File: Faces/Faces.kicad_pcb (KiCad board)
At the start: 6 copper layers, 120.8 x 142.1 mm, 92 parts

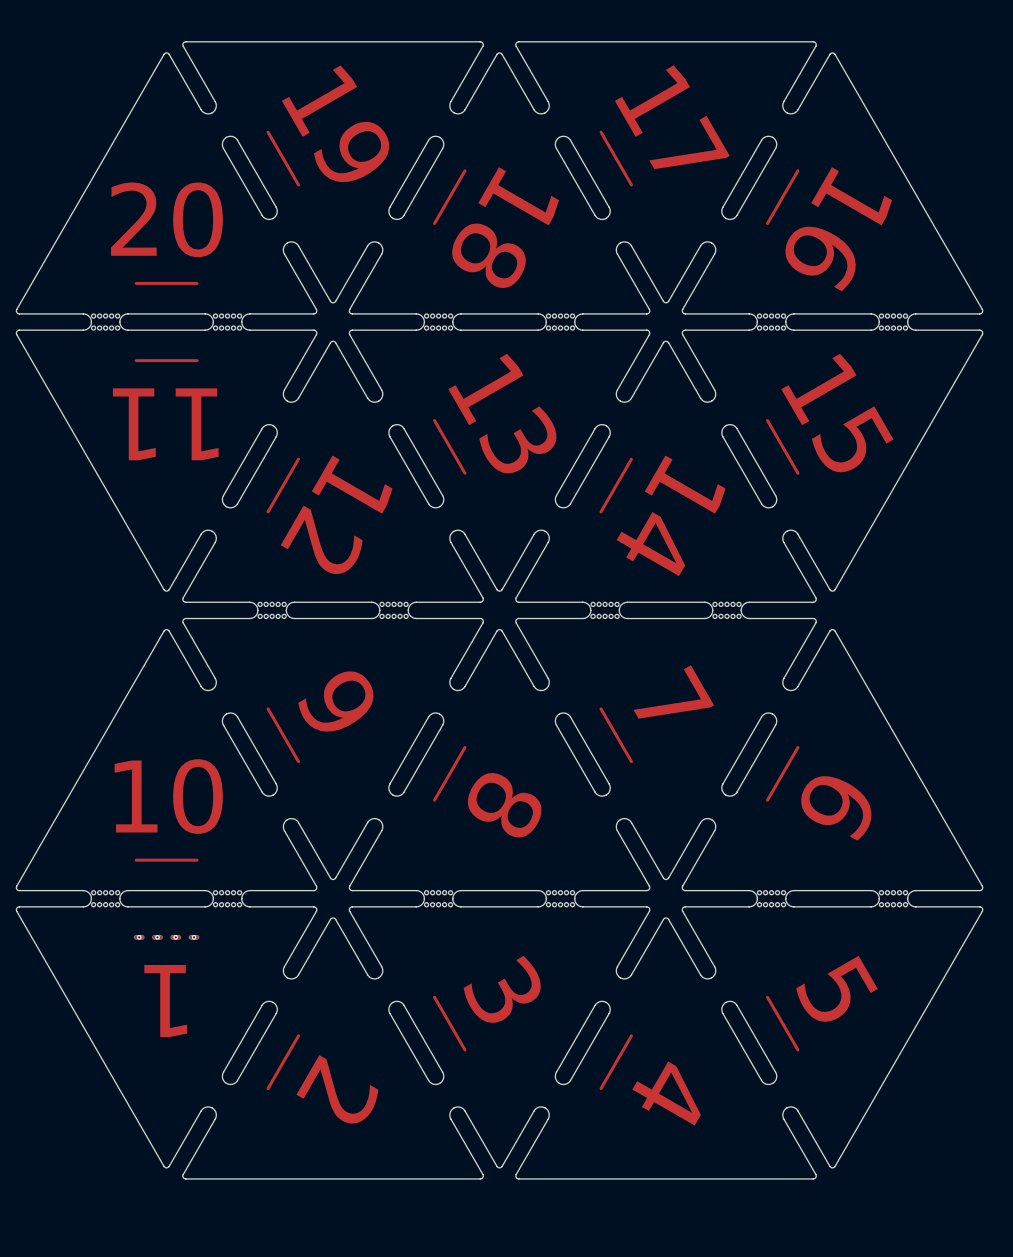
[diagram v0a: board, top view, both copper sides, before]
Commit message: Re-tool faces. It costs nothing to add the extra panelization holes. They bill this as 20 designs regardless.
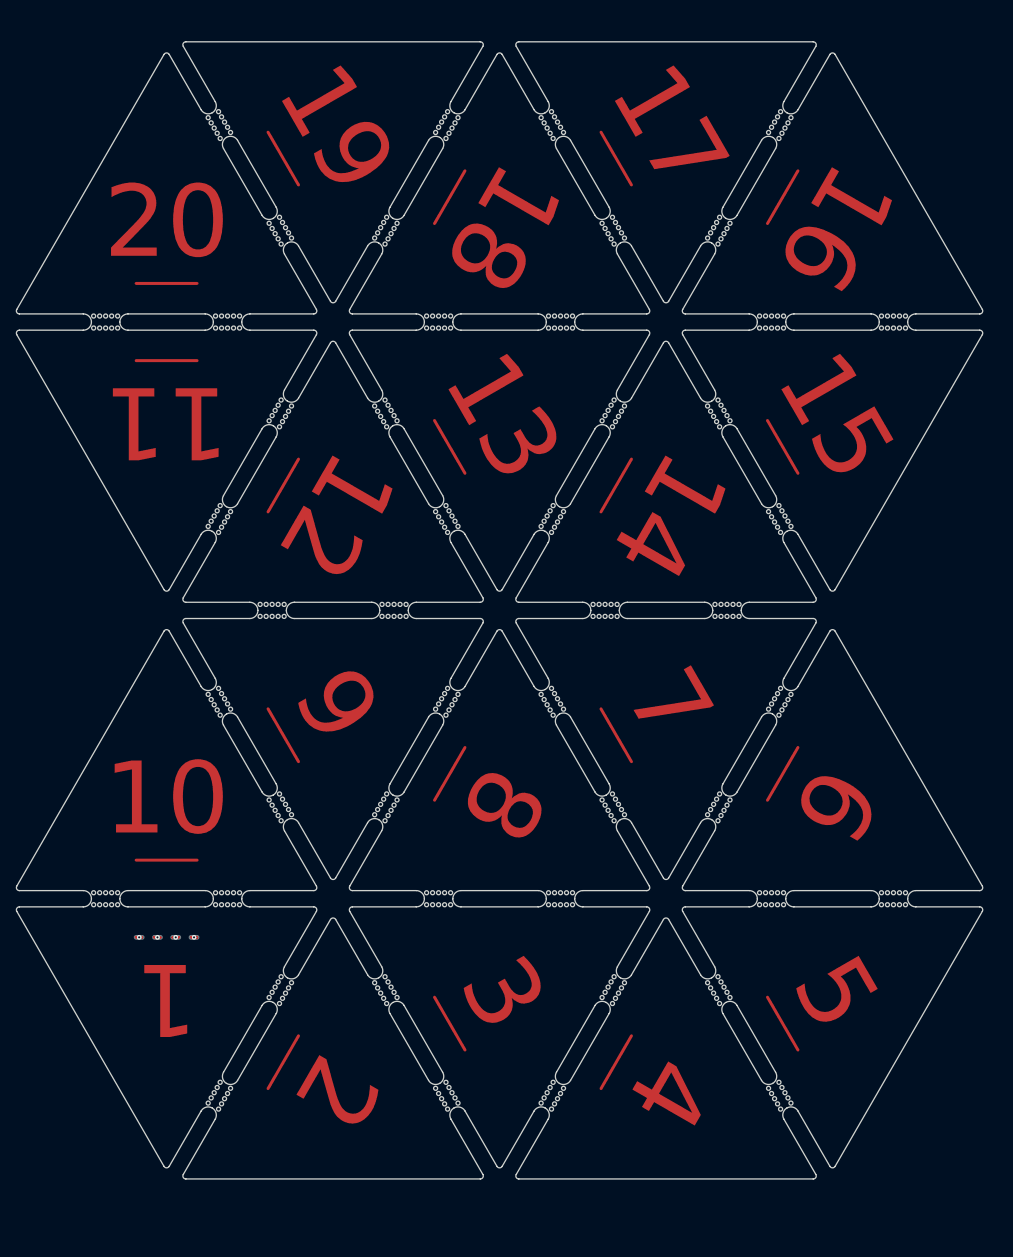
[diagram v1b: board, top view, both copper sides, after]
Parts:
- added mouse-bite-2mm-slot (x2): VAL**, Panelization:mouse-bite-2mm-slot, F.Cu at (78.2, 63.2)
- added mouse-bite-2mm-slot (x2): VAL**, Panelization:mouse-bite-2mm-slot, F.Cu at (127.4, 148.5)
- added mouse-bite-2mm-slot (x2): VAL**, Panelization:mouse-bite-2mm-slot, F.Cu at (65.0, 135.3)
- added mouse-bite-2mm-slot (x2): VAL**, Panelization:mouse-bite-2mm-slot, F.Cu at (85.8, 99.3)
- added mouse-bite-2mm-slot (x2): VAL**, Panelization:mouse-bite-2mm-slot, F.Cu at (65.0, 40.4)
- added mouse-bite-2mm-slot (x2): VAL**, Panelization:mouse-bite-2mm-slot, F.Cu at (65.0, 63.2)
- added mouse-bite-2mm-slot (x2): VAL**, Panelization:mouse-bite-2mm-slot, F.Cu at (127.4, 99.3)
- added mouse-bite-2mm-slot (x2): VAL**, Panelization:mouse-bite-2mm-slot, F.Cu at (106.6, 63.2)
- added mouse-bite-2mm-slot (x2): VAL**, Panelization:mouse-bite-2mm-slot, F.Cu at (57.4, 99.3)
- added mouse-bite-2mm-slot (x2): VAL**, Panelization:mouse-bite-2mm-slot, F.Cu at (57.4, 76.4)
- added mouse-bite-2mm-slot (x2): VAL**, Panelization:mouse-bite-2mm-slot, F.Cu at (106.6, 112.5)
- added mouse-bite-2mm-slot (x2): VAL**, Panelization:mouse-bite-2mm-slot, F.Cu at (99.0, 148.5)
- added mouse-bite-2mm-slot (x2): VAL**, Panelization:mouse-bite-2mm-slot, F.Cu at (85.8, 148.5)
- added mouse-bite-2mm-slot (x2): VAL**, Panelization:mouse-bite-2mm-slot, F.Cu at (57.4, 148.5)
- added mouse-bite-2mm-slot (x2): VAL**, Panelization:mouse-bite-2mm-slot, F.Cu at (85.8, 76.4)
- added mouse-bite-2mm-slot (x2): VAL**, Panelization:mouse-bite-2mm-slot, F.Cu at (119.8, 112.5)
- added mouse-bite-2mm-slot (x2): VAL**, Panelization:mouse-bite-2mm-slot, F.Cu at (119.8, 63.2)
- added mouse-bite-2mm-slot (x2): VAL**, Panelization:mouse-bite-2mm-slot, F.Cu at (106.6, 40.4)
- added mouse-bite-2mm-slot (x2): VAL**, Panelization:mouse-bite-2mm-slot, F.Cu at (78.2, 135.3)
- added mouse-bite-2mm-slot (x2): VAL**, Panelization:mouse-bite-2mm-slot, F.Cu at (127.4, 27.2)
- added mouse-bite-2mm-slot (x2): VAL**, Panelization:mouse-bite-2mm-slot, F.Cu at (119.8, 40.4)
- added mouse-bite-2mm-slot (x2): VAL**, Panelization:mouse-bite-2mm-slot, F.Cu at (65.0, 112.5)
- added mouse-bite-2mm-slot (x2): VAL**, Panelization:mouse-bite-2mm-slot, F.Cu at (85.8, 27.2)
- added mouse-bite-2mm-slot (x2): VAL**, Panelization:mouse-bite-2mm-slot, F.Cu at (127.4, 76.4)
- added mouse-bite-2mm-slot (x2): VAL**, Panelization:mouse-bite-2mm-slot, F.Cu at (119.8, 135.3)
- added mouse-bite-2mm-slot (x2): VAL**, Panelization:mouse-bite-2mm-slot, F.Cu at (57.4, 27.2)
- added mouse-bite-2mm-slot (x2): VAL**, Panelization:mouse-bite-2mm-slot, F.Cu at (99.0, 76.4)
- added mouse-bite-2mm-slot (x2): VAL**, Panelization:mouse-bite-2mm-slot, F.Cu at (99.0, 99.3)
- added mouse-bite-2mm-slot (x2): VAL**, Panelization:mouse-bite-2mm-slot, F.Cu at (106.6, 135.3)
- added mouse-bite-2mm-slot (x2): VAL**, Panelization:mouse-bite-2mm-slot, F.Cu at (99.0, 27.2)
- added mouse-bite-2mm-slot (x2): VAL**, Panelization:mouse-bite-2mm-slot, F.Cu at (78.2, 40.4)
- added mouse-bite-2mm-slot (x2): VAL**, Panelization:mouse-bite-2mm-slot, F.Cu at (78.2, 112.5)
- moved G*** 3.59 mm to (109.5, 93.1), turned to -55 degrees
- moved G*** 3.10 mm to (68.2, 91.4), turned to -65 degrees
- moved G*** 2.73 mm to (60.4, 137.8)
- moved G*** 2.61 mm to (138.9, 103.7), turned to -125 degrees
- moved G*** 2.10 mm to (139.5, 31.4), turned to -125 degrees
- moved G*** 2.07 mm to (108.8, 18.8), turned to -65 degrees
- moved G*** 1.97 mm to (40.6, 111.9), turned to -5 degrees
- moved G*** 1.91 mm to (97.9, 31.2), turned to -125 degrees
- moved G*** 1.84 mm to (67.4, 18.3), turned to -65 degrees
- moved G*** 1.67 mm to (98.0, 103.0), turned to -125 degrees
- moved G*** 1.55 mm to (41.0, 137.4)
- moved G*** 1.03 mm to (77.5, 66.4)
- moved G*** 0.70 mm to (62.2, 64.3)
- moved G*** 0.51 mm to (39.0, 39.5)

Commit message: Somewhere around the first complete prototype. time to change BMS
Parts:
- moved G*** 152.7 mm to (119.2, 161.9), turned to 115 degrees
- moved G*** 149.4 mm to (47.1, 148.8), turned to 55 degrees
- moved G*** 148.4 mm to (147.6, 140.7), turned to 170 degrees
- moved G*** 146.0 mm to (77.8, 161.5), turned to 115 degrees
- moved mouse-bite-2mm-slot 144.9 mm to (129.2, 153.1), turned to 120 degrees
- moved mouse-bite-2mm-slot 144.9 mm to (129.2, 153.1), turned to -60 degrees
- moved mouse-bite-2mm-slot 143.2 mm to (59.1, 153.1), turned to 60 degrees
- moved mouse-bite-2mm-slot 143.2 mm to (59.1, 153.1), turned to -120 degrees
- moved G*** 143.2 mm to (117.2, 22.7), turned to 115 degrees
- moved G*** 141.0 mm to (145.6, 42.8), turned to 55 degrees
- moved G*** 140.4 mm to (46.1, 38.1), turned to 175 degrees
- moved G*** 137.6 mm to (75.6, 23.7), turned to 115 degrees
- moved mouse-bite-2mm-slot 137.1 mm to (129.2, 31.7), turned to -120 degrees
- moved mouse-bite-2mm-slot 137.1 mm to (129.2, 31.7), turned to 60 degrees
- moved mouse-bite-2mm-slot 135.3 mm to (59.1, 31.7), turned to -60 degrees
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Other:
- board text added: "DIO"
- board text added: "GND"
- board text added: "SCK"
- board text added: "VBUS"
